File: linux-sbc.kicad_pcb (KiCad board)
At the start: 8 copper layers, 524 parts, among them J1001 7499010121A, J101 Mini-fit Jr 5569, J1101 DM3AT-SF-PEJM5, J1201 PH1-08-UA, J1202 EMI shield frame, J1203 FH12A-40S-0.5SH(55), J1301 SMA RF2-04, J201 61300211121, J202 61300211121, J203 61300211121, J204 61300211121, J205 61300211121, J206 61300211121, J207 61300211121, J208 61300211121, J301 61300211121, J302 61300211121, J303 EMI shield frame, J401 Conn_01x04, J402 EMI shield frame, J701 USB4105-GF-A, J702 TC2050-NL, J901 AU-Y1008-2-BLK, J902 AU-Y1008-2-BLK, Q201 DMPH4029LFGQ, Q202 DMPH4029LFGQ, Q203 DMN65D8L, Q204 DMPH4029LFGQ, Q205 DMPH4029LFGQ, SW501 JS202011CQN, U1001 LAN8742A-CZ-TR, U1201 TCA9554PW, U1202 AP5725FDCG-7, U1301 LBEE5KL1YN-814, U201 LM4040-5.0, U202 TL331, U203 OPA197, U204 LM4040-5.0, U205 TL331, U206 LM4040-5.0, U207 TL331, U301 AP64500SP-13, U302 AP64500SP-13, U401 STPMIC1DPQR, U501 STM32MP135FAE7, U701 FT231XQ-R, U702 TCA9554PW, U801 MT41K256M16TW, U901 USB2514B/M2, U902 AP22966DC8-7, U903 AP22966DC8-7, Y501 32.768 kHz, Y502 24 MHz, Y901 24 MHz

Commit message: Refactor peripheral routing
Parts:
- moved R703 0.70 mm to (-42.7, -195.8)
- moved C701 0.64 mm to (-47.3, -188.4)
- moved R1012 0.40 mm to (-102.0, -184.3)
- moved R1014 0.40 mm to (-100.5, -184.3)
- moved R1015 0.20 mm to (-99.5, -184.3)
- moved R1016 0.20 mm to (-98.0, -184.3)
- moved C1301 0.13 mm to (153.6, -184.6)
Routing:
- net /User Interface/V_BL_A: track 20.7 -> 19.5 mm
- net /Ethernet/TX_P: track 18.9 -> 20.0 mm
- net /Ethernet/TX_N: track 19.0 -> 20.1 mm
- net /Debug/RTCK: track 3.37 -> 2.67 mm
- net /Debug/VDD: track 27.8 -> 27.2 mm
- net GND: vias 477 -> 479

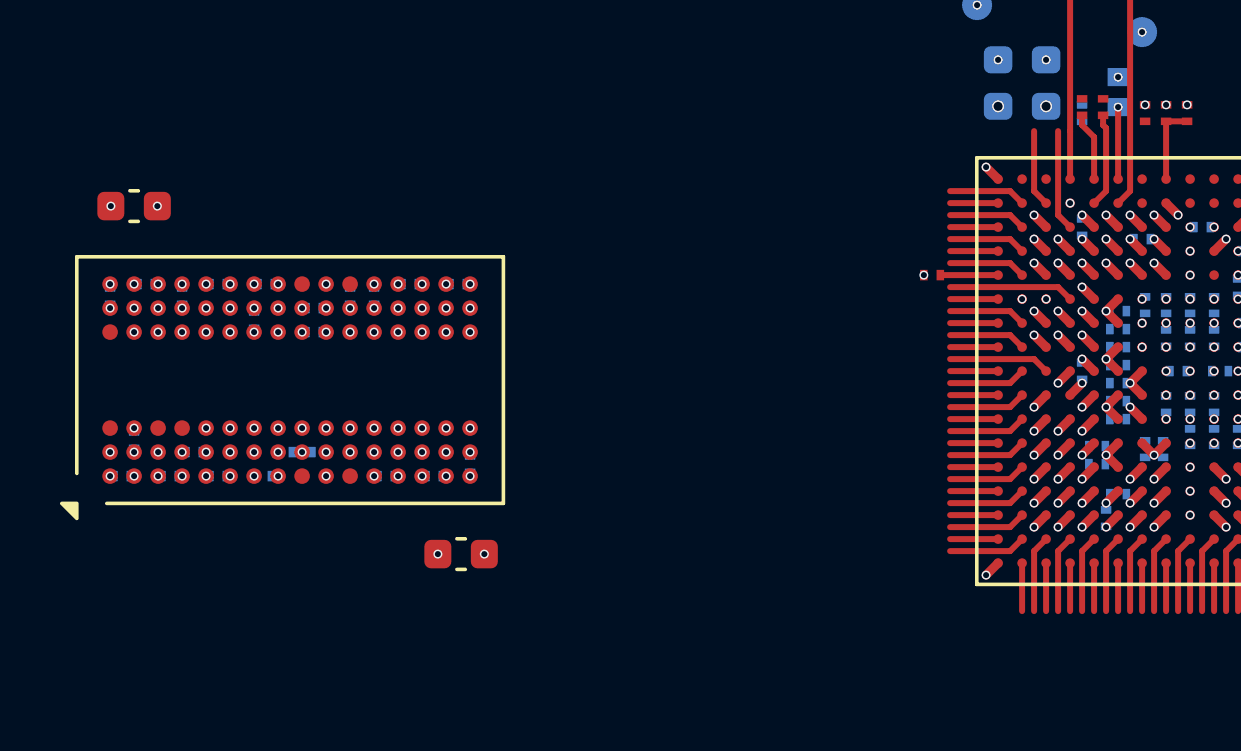
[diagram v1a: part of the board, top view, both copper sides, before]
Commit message: Update impedance calculations
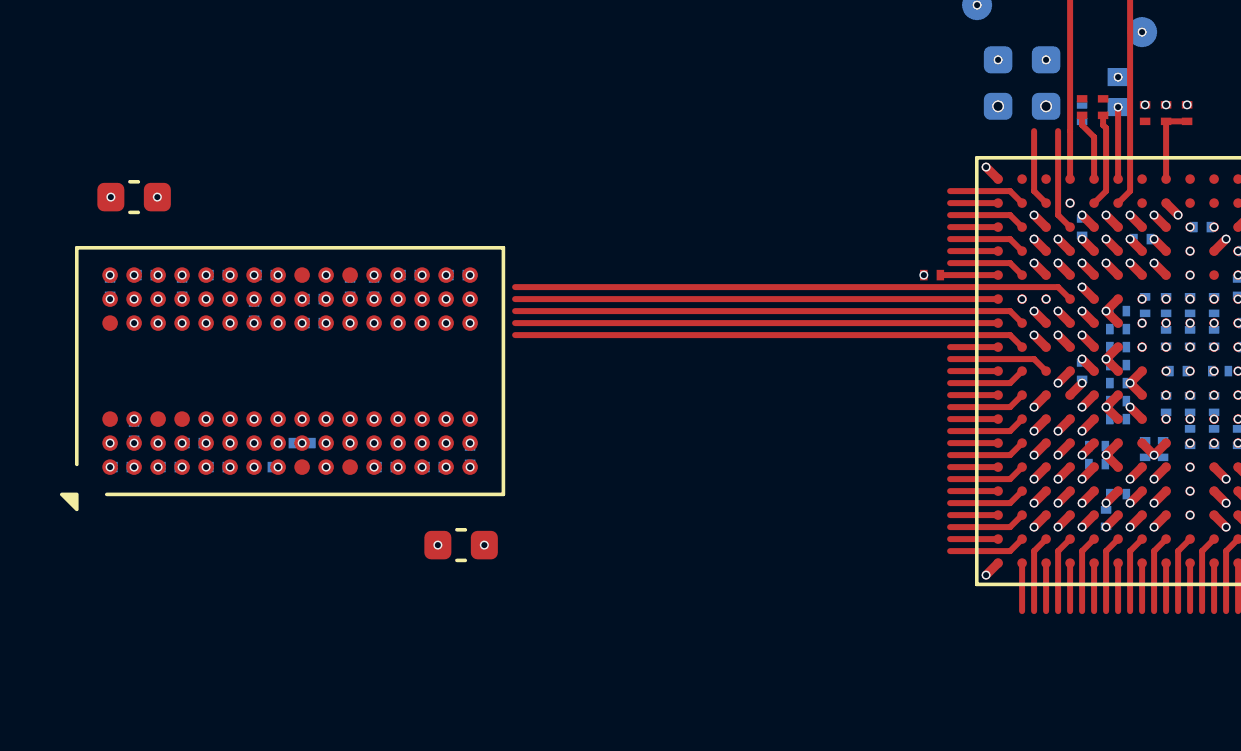
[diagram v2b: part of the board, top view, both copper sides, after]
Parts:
- moved C818 0.30 mm to (-329.2, 97.6)
- moved C801 0.30 mm to (-335.2, 94.2)
- moved C802 0.30 mm to (-324.3, 105.8)
- moved C803 0.30 mm to (-335.2, 102.0)
- moved C804 0.30 mm to (-335.6, 103.2)
- moved C805 0.30 mm to (-333.6, 97.2)
- moved C806 0.30 mm to (-336.0, 97.2)
- moved C808 0.30 mm to (-331.2, 98.0)
- moved C809 0.30 mm to (-334.0, 103.2)
- moved C813 0.30 mm to (-329.0, 102.4)
- moved C814 0.30 mm to (-334.8, 96.8)
- moved C819 0.30 mm to (-333.2, 102.4)
- moved C823 0.30 mm to (-326.8, 103.2)
- moved C824 0.30 mm to (-332.4, 96.8)
- moved C828 0.30 mm to (-330.9, 103.2)
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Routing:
- net /DDR/DDR.BA1: track 2.57 -> 17.1 mm
- net /DDR/DDR.A6: track 1.60 -> 16.1 mm
- net /DDR/DDR.A4: track 4.17 -> 18.7 mm
- net /DDR/DDR.A14: track 1.60 -> 16.1 mm
- net /DDR/DDR.A15: track 2.57 -> 17.1 mm

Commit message: DDR AC first iteration
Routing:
- net /DDR/DDR.CKE: track 0.57 -> 31.2 mm
- net /DDR/DDR.A3: track 0.57 -> 26.9 mm
- net /DDR/DDR.WE_N: track 0.57 -> 26.5 mm
- net /DDR/DDR.ODT: track 0.57 -> 26.3 mm
- net /DDR/DDR.BA2: track 0.57 -> 25.9 mm
- net /DDR/DDR.A10: track 0.57 -> 25.6 mm
- net /DDR/DDR.RAS_N: track 1.60 -> 24.6 mm, vias 1 -> 0
- net /DDR/DDR.A7: track 0.57 -> 23.4 mm, vias 2 -> 4
- net /DDR/DDR.CLK_P: track 2.57 -> 25.2 mm
- net /DDR/DDR.A13: track 0.57 -> 23.0 mm
- net /DDR/DDR.CAS_N: track 3.37 -> 25.6 mm, vias 1 -> 2
- net /DDR/DDR.CLK_N: track 1.60 -> 23.6 mm
- net /DDR/DDR.A11: track 0.57 -> 22.3 mm
- net /DDR/DDR.CS_N: track 2.57 -> 24.0 mm, vias 1 -> 2
- net /DDR/DDR.A1: track 0.57 -> 21.9 mm
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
